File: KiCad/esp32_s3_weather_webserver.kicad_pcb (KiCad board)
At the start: 4 copper layers, 85 x 75 mm, 129 parts, among them IC301 CP2102N-A02-GQFN28R, IC401 ESP32-S3-WROOM-1-N16R8, IC501 VEML7700-TT, IC502 DS3231MZ+TRL, J201 Barrel_Jack_Switch_Pin3Ring, J301 USB_C_Receptacle_USB2.0, J302 USB_C_Receptacle_USB2.0, J401 Conn_01x04_Pin, J402 Conn_01x04_Pin, J403 Conn_01x04_Pin, J404 TF-01A, J405 Conn_01x06_Pin, Q401 SS8050, Q402 SS8050, U201 AMS1117-3.3, U202 TLV62569DBV, U301 USBLC6-2SC6, U302 USBLC6-2SC6, U502 DS18B20, U503 LM35-LP, U504 DHT11

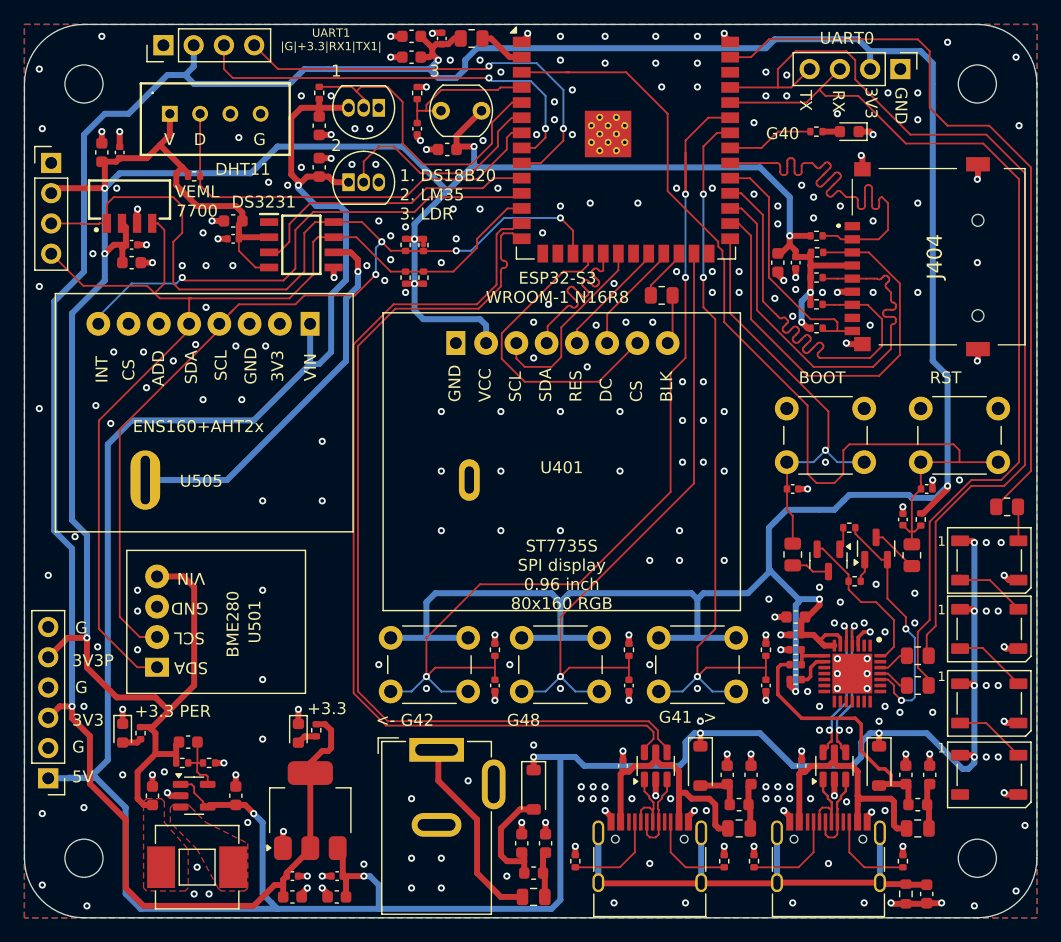
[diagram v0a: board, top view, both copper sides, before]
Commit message: Add battery connector and charger
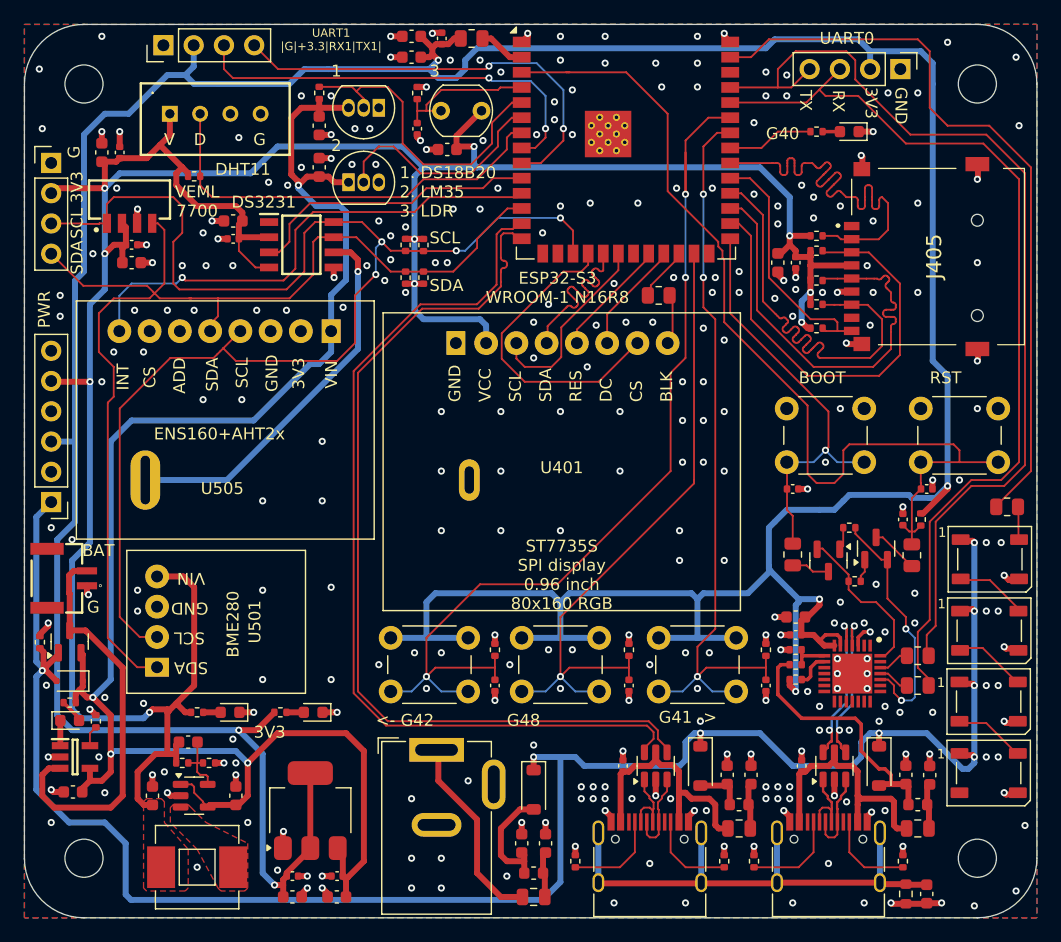
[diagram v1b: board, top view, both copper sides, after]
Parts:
- added C214: 22uF, Capacitor_SMD:C_0603_1608Metric, F.Cu at (29.1, 89.4)
- added D211: LED, LED_SMD:LED_0603_1608Metric, F.Cu at (42.3, 82.8)
- added D212: LED, LED_SMD:LED_0603_1608Metric, F.Cu at (94.2, 34.0)
- added IC201: MCP73831T-2ACI_OT, esp32_s3_weather_webserver:SOT95P270X145-5N, F.Cu at (29.2, 86.5)
- added J202: BM02B-GHS-TBT_LF__SN__N_, esp32_s3_weather_webserver:BM02B-GHS-TBT_1, F.Cu at (30.2, 71.5)
- added Q201: DMG3415U-7, Package_TO_SOT_SMD:SOT-23, F.Cu at (28.8, 76.8)
- added R207: 510R, Resistor_SMD:R_0402_1005Metric, F.Cu at (46.5, 82.8)
- added R208: 510R, Resistor_SMD:R_0402_1005Metric, F.Cu at (39.5, 82.8)
- added R209: 510R, Resistor_SMD:R_0402_1005Metric, F.Cu at (91.5, 34.0)
- C207, C208: value 22uF -> 2.2uF
- C209: value DNP -> 22uF
- C210: value 2.2uF -> 22uF
- C211: value 2.2uF -> DNP
- D204: value WS2812B -> PMEG1030EJ,115; footprint LED_SMD:LED_WS2812B_PLCC4_5.0x5.0mm_P3.2mm -> Diode_SMD:D_SOD-323F
- D205: value WS2812B -> LED; footprint LED_SMD:LED_WS2812B_PLCC4_5.0x5.0mm_P3.2mm -> LED_SMD:LED_0603_1608Metric
- D208, D209: value LED -> WS2812B; footprint LED_SMD:LED_0603_1608Metric -> LED_SMD:LED_WS2812B_PLCC4_5.0x5.0mm_P3.2mm
- J404: value TF-01A -> Conn_01x06_Pin; footprint esp32_s3_weather_webserver:TF01A -> Connector_PinHeader_2.54mm:PinHeader_1x06_P2.54mm_Vertical
- J405: value Conn_01x06_Pin -> TF-01A; footprint Connector_PinHeader_2.54mm:PinHeader_1x06_P2.54mm_Vertical -> esp32_s3_weather_webserver:TF01A
- R203: value 0R -> 510R; footprint Resistor_SMD:R_0805_2012Metric -> Resistor_SMD:R_0402_1005Metric
- R204: value 510R -> 5k1R
- R205: value 510R -> 100kR
- R206: value 510R -> 0R; footprint Resistor_SMD:R_0402_1005Metric -> Resistor_SMD:R_0805_2012Metric
- R409: value 10kR -> 0R; footprint Resistor_SMD:R_0402_1005Metric -> Resistor_SMD:R_0805_2012Metric
- R414: value 0R -> 10kR; footprint Resistor_SMD:R_0805_2012Metric -> Resistor_SMD:R_0402_1005Metric
- moved J405 86.6 mm to (101.7, 44.5), turned to 90 degrees
- moved R203 80.4 mm to (28.8, 81.9), turned to 0 degrees
- moved D204 77.9 mm to (28.8, 80.1), turned to 180 degrees
- moved D205 77.6 mm to (28.8, 83.4)
- moved J404 77.3 mm to (27.2, 65.1), turned to 180 degrees
- moved D209 72.8 mm to (106.0, 87.8), turned to 0 degrees
- moved D210 66.4 mm to (49.2, 82.8)
- moved C210 65.3 mm to (35.8, 89.8)
- moved C208 63.3 mm to (99.0, 88.0)
- moved C211 60.3 mm to (38.8, 85.2), turned to 0 degrees
- moved C207 58.3 mm to (101.0, 88.0)
- moved D208 58.0 mm to (106.0, 81.8), turned to 0 degrees
- moved R206 35.3 mm to (107.5, 65.5)
- moved R204 18.5 mm to (31.0, 83.5)
- moved R414 13.3 mm to (91.5, 50.5)
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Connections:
- C201 pad 1: +5V -> VIN
- C202 pad 1: +5V -> VIN
- C207 pad 1: +5V -> +VCC_USB2UART_FUSE
- C208 pad 1: +3V3_PER -> +VCC_USB2UART_FILT
- C209 pad 1: +3V3_PER -> VIN
- C209 pad 2: /[2] Power/BUCK_FB -> GND
- C210 pad 1: +VCC_USB2UART_FUSE -> +3V3_PER
- C211 pad 1: +VCC_USB2UART_FILT -> +3V3_PER
- C211 pad 2: GND -> /[2] Power/BUCK_FB
- C505 pad 1: +5V -> VIN
- C506 pad 1: +5V -> VIN
- D204 pad 1: +5V -> VIN
- D204 pad 2: Net-(D204-DOUT) -> +5V
- D205 pad 1: +5V -> /[2] Power/STAT
- D205 pad 2: Net-(D205-DOUT) -> /[2] Power/LED_STAT_A
- D206 pad 4: Net-(D205-DOUT) -> Net-(D206-DIN)
- D207 pad 2: unconnected-(D207-DOUT-Pad2) -> Net-(D207-DOUT)
- D208 pad 1: GND -> +5V
- D208 pad 2: /[2] Power/LED_3V3_A -> Net-(D208-DOUT)
- D209 pad 1: GND -> +5V
- D209 pad 2: /[2] Power/LED_3V3_PER_A -> unconnected-(D209-DOUT-Pad2)
- D210 pad 2: /[2] Power/LED_ONBOARD_A -> /[2] Power/LED_3V3_A
- J404 pad 1: unconnected-(J404-D2/X-Pad1) -> +5V
- J404 pad 2: FSPI_SS -> GND
- J404 pad 3: FSPI_MOSI -> +3V3
- J404 pad 4: +3V3_PER -> GND
- J404 pad 5: FSPI_SCK -> +3V3_PER
- J405 pad 1: +5V -> unconnected-(J405-D2/X-Pad1)
- J405 pad 2: GND -> FSPI_SS
- J405 pad 3: +3V3 -> FSPI_MOSI
- J405 pad 4: GND -> +3V3_PER
- J405 pad 5: +3V3_PER -> FSPI_SCK
- R203 pad 1: Net-(D204-DIN) -> /[2] Power/LED_STAT_A
- R203 pad 2: WS2812_RGB_STRIP -> VIN
- R204 pad 1: /[2] Power/LED_3V3_A -> /[2] Power/PROG
- R204 pad 2: +3V3 -> GND
- R205 pad 1: /[2] Power/LED_3V3_PER_A -> GND
- R205 pad 2: +3V3_PER -> +5V
- R206 pad 1: /[2] Power/LED_ONBOARD_A -> Net-(D206-DIN)
- R206 pad 2: ONBOARD_LED -> WS2812_RGB_STRIP
- R409 pad 1: FSPI_MISO -> Net-(U401-BLK)
- R409 pad 2: +3V3_PER -> TFT_BLK
- R410 pad 1: FSPI_MOSI -> FSPI_MISO
- R411 pad 1: FSPI_SCK -> FSPI_MOSI
- R412 pad 1: FSPI_SS -> FSPI_SCK
- R413 pad 1: SD_CD -> FSPI_SS
- R414 pad 1: Net-(U401-BLK) -> SD_CD
- R414 pad 2: TFT_BLK -> +3V3_PER
- R504 pad 1: +5V -> VIN
- U201 pad 3: +5V -> VIN
- U202 pad 1: +5V -> VIN
- U202 pad 4: +5V -> VIN
- U502 pad 3: +5V -> VIN
- U503 pad 1: +5V -> VIN
- U505 pad 1: +5V -> VIN
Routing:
- net VIN: track 0.00 -> 144.8 mm, vias 0 -> 4
- net +5V: track 251.5 -> 162.9 mm, vias 10 -> 8
- net VBAT: track 0.00 -> 33.9 mm
- net Net-(D207-DOUT): track 0.00 -> 6.14 mm
- net Net-(D205-DOUT): track 6.14 -> 0.00 mm
- net Net-(D204-DOUT): track 6.06 -> 0.00 mm
- net Net-(D208-DOUT): track 0.00 -> 6.02 mm
- net I2C_SCL: track 112.8 -> 118.2 mm
- net GND: track 75.4 -> 80.3 mm, vias 307 -> 313
- net I2C_SDA: track 92.8 -> 97.2 mm
- net +3V3: track 333.3 -> 329.9 mm, vias 5 -> 6
- net Net-(D206-DIN): track 0.00 -> 2.47 mm
- net Net-(D204-DIN): track 2.47 -> 0.00 mm
- net /[2] Power/STAT: track 0.00 -> 2.12 mm
- net +3V3_PER: track 239.1 -> 241.2 mm, vias 9 -> 10
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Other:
- board text added: "BAT"
- board text added: "PWR"
- board text added: "SCL"
- board text added: "SDA"
- board text removed: "+3.3"
- board text removed: "+3.3 PER"
- board text removed: "3V3P"
- board text removed: "5V"

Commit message: Connect VBAT to ADC input to measure battery voltage
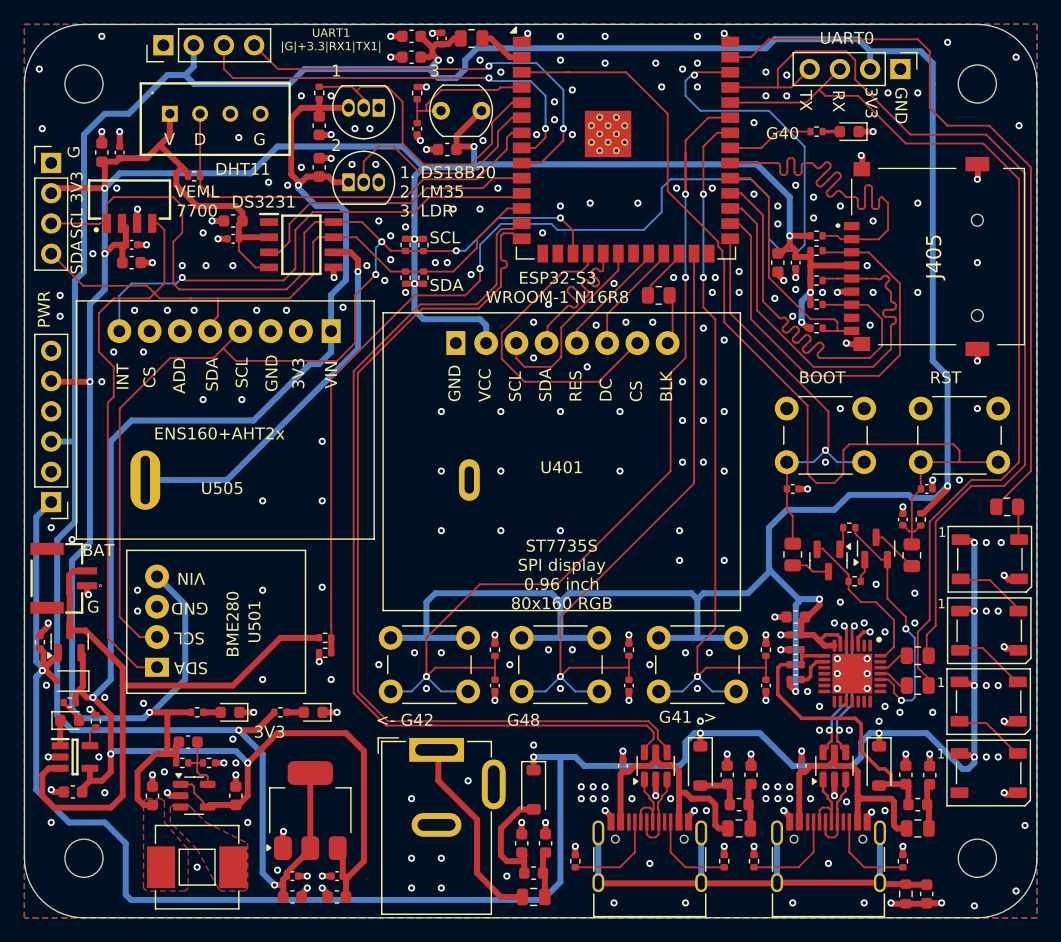
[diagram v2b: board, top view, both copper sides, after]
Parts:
- added R210: 100kR, Resistor_SMD:R_0402_1005Metric, F.Cu at (50.2, 76.5)
- added R211: 100kR, Resistor_SMD:R_0402_1005Metric, F.Cu at (50.2, 77.8)
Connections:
- IC401 pad 38: unconnected-(IC401-IO2-Pad38) -> VBAT_STAT
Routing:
- net VBAT_STAT: track 0.00 -> 103.1 mm, vias 0 -> 2
- net VBAT: track 33.9 -> 52.0 mm
- net +3V3_PER: track 241.2 -> 240.4 mm
- net GND: track 80.3 -> 81.0 mm, vias 313 -> 316

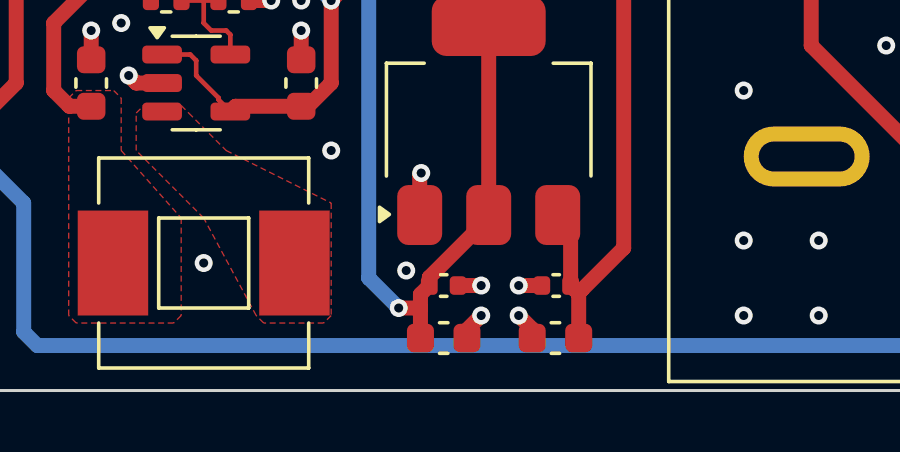
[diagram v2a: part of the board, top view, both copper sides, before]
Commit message: Use tantalum capacitor with AMS. Add basic output to TFT.
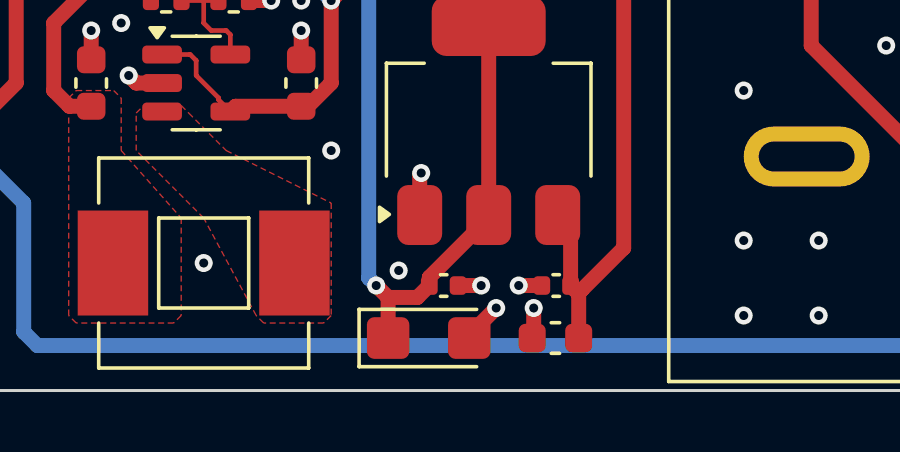
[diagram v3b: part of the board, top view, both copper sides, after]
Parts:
- C204: value 10uF -> 22uF_P; footprint Capacitor_SMD:C_0603_1608Metric -> Capacitor_Tantalum_SMD:CP_EIA-3216-18_Kemet-A
- moved C204 0.50 mm to (47.0, 98.2)
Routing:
- net GND: track 81.0 -> 81.6 mm

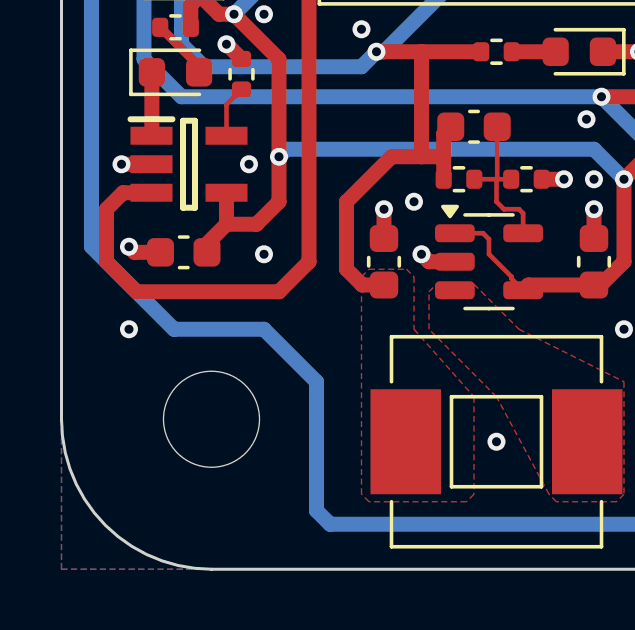
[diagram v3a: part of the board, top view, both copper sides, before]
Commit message: VBAT decoupling capacitor
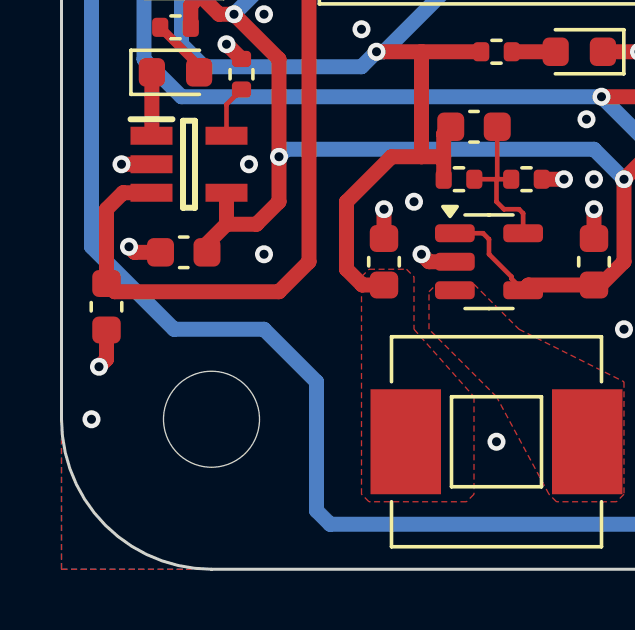
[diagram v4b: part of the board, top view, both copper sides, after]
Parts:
- added C215: 22uF, Capacitor_SMD:C_0603_1608Metric, F.Cu at (26.5, 91.2)
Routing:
- net GND: track 81.6 -> 82.9 mm, vias 316 -> 317

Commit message: Production files prepare
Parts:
- moved C215 2.24 mm to (27.5, 89.2), turned to 0 degrees
- moved C214 1.93 mm to (31.0, 89.2)
- moved R206 1.27 mm to (106.2, 65.8)
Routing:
- net /[4] ESP32 S3/RXD0: track 78.1 -> 68.5 mm
- net /[4] ESP32 S3/TXD0: track 81.0 -> 72.0 mm
- net /[4] ESP32 S3/CHIP_PU: track 81.5 -> 76.1 mm
- net VBAT_STAT: track 103.1 -> 100.5 mm
- net USR_BTN_LEFT: track 81.5 -> 83.7 mm, vias 3 -> 2
- net +3V3_PER: track 240.4 -> 242.3 mm
- net I2C_SCL: track 118.2 -> 119.5 mm
- net VIN: track 144.8 -> 143.6 mm
- net +3V3: track 329.7 -> 328.6 mm
- net /[3] USB/USB2UART_D-: track 13.8 -> 14.9 mm
- net /[3] USB/USB2UART_D+: track 13.7 -> 14.5 mm
- net Net-(D206-DIN): track 2.47 -> 3.25 mm
- net +5V_IN_FILT: track 9.65 -> 8.99 mm
- net WS2812_RGB_STRIP: track 62.8 -> 62.2 mm
- net RXD1: track 35.8 -> 36.4 mm
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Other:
- board text added: "+3V3"
- board text added: "+5V"
- board text added: "UART"
- board text added: "USB"
